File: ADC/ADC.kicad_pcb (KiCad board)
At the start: 2 copper layers, 57 x 82.4 mm, 78 parts, among them IC1 ADS7953SDBT, IC2 REF5025ID, IC3 ADS7953SDBT, IC4 REF5025ID, IC5 ADP3338AKCZ-5-REEL, J1 USB_C_Receptacle_USB2.0, J2 Conn_01x04_MountingPin, J3 Conn_02x11_Odd_Even, J4 Conn_02x08_Top_Bottom, J5 Conn_02x08_Top_Bottom, J6 Conn_01x04_MountingPin, J7 Conn_02x05_Odd_Even, U1 STM32F072CBT6, U2 OPA192ID, U3 PRTR5V0U2X, U4 XC6206PxxxMR-Regulator_Linear, U5 OPA192ID

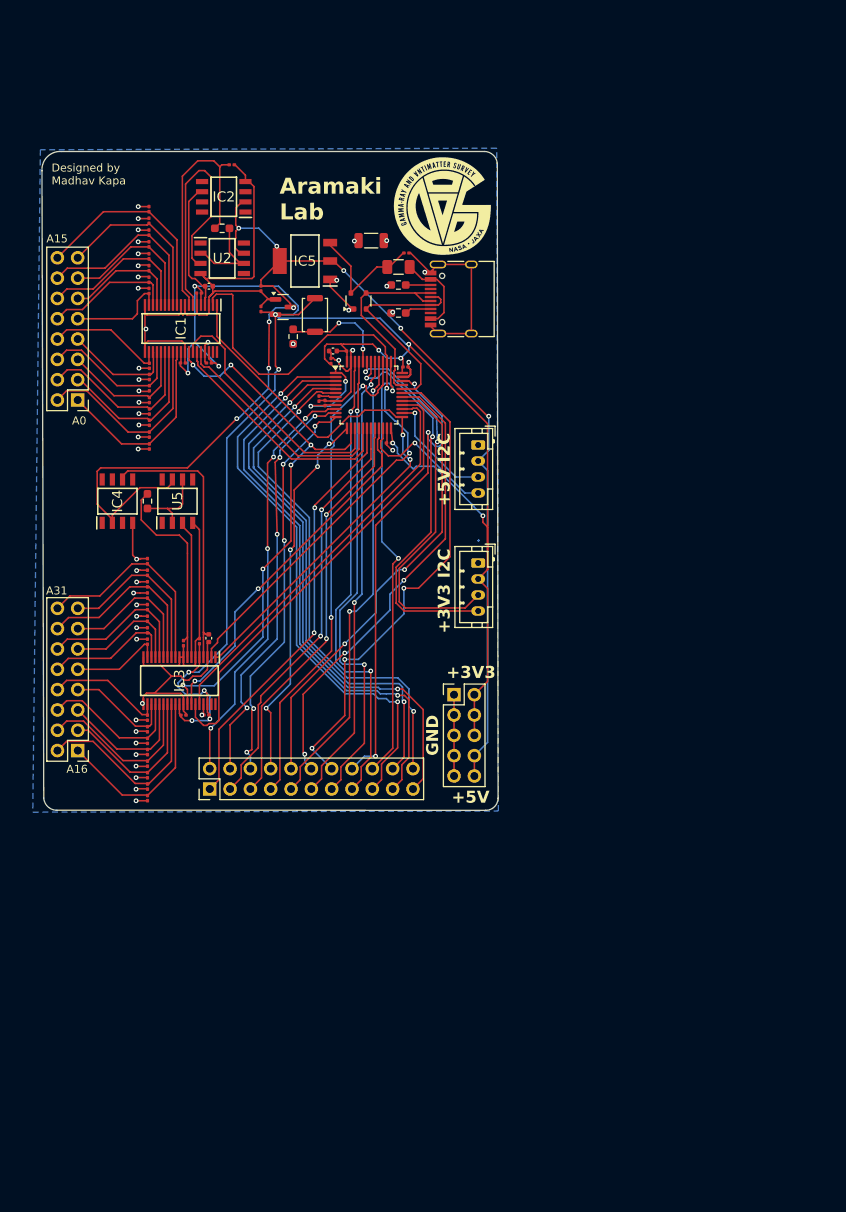
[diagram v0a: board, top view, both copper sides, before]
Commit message: updated schematic to match the eval kit
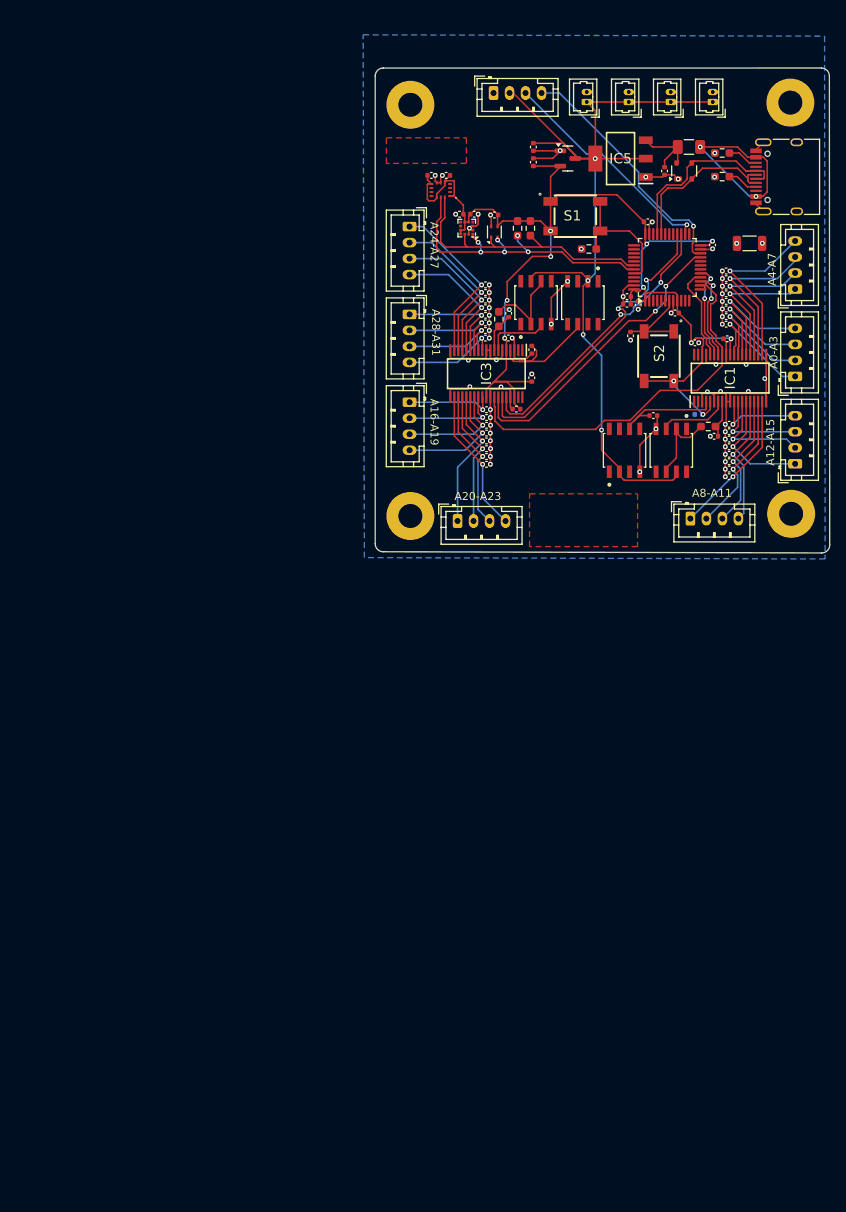
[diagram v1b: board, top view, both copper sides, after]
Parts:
- removed J3: Conn_02x11_Odd_Even, Connector_PinHeader_2.54mm:PinHeader_2x11_P2.54mm_Vertical
- removed J7: Conn_02x05_Odd_Even, Connector_PinHeader_2.54mm:PinHeader_2x05_P2.54mm_Vertical
- removed SW1: ~, Button_Switch_SMD:SW_Push_SPST_NO_Alps_SKRK
- added AC1: LSM6DSOTR, SamacSys_Parts:LGA-14_2.5X3X0.86_, F.Cu at (75.0, 34.2)
- added C53: 100nF, Capacitor_SMD:C_0402_1005Metric, F.Cu at (81.7, 37.4)
- added C54: 100nF, Capacitor_SMD:C_0402_1005Metric, F.Cu at (79.2, 37.2)
- added C56: 220nF, Capacitor_SMD:C_0402_1005Metric, F.Cu at (77.3, 37.2)
- added C57: 100nF, Capacitor_SMD:C_0402_1005Metric, F.Cu at (73.8, 32.4)
- added C58: 100nF, Capacitor_SMD:C_0402_1005Metric, F.Cu at (75.7, 32.4)
- added H1: MountingHole_Pad, MountingHole:MountingHole_3mm_Pad, F.Cu at (118.7, 23.3)
- added H2: MountingHole_Pad, MountingHole:MountingHole_3mm_Pad, F.Cu at (71.2, 75.0)
- added H3: MountingHole_Pad, MountingHole:MountingHole_3mm_Pad, F.Cu at (71.2, 23.6)
- added H4: MountingHole_Pad, MountingHole:MountingHole_3mm_Pad, F.Cu at (118.8, 74.7)
- added J10: Conn_01x04_MountingPin, Connector_JST:JST_PH_B4B-PH-K_1x04_P2.00mm_Vertical, F.Cu at (119.3, 68.5)
- added J11: Conn_01x04_MountingPin, Connector_JST:JST_PH_B4B-PH-K_1x04_P2.00mm_Vertical, F.Cu at (77.1, 75.6)
- added J12: Conn_01x04_MountingPin, Connector_JST:JST_PH_B4B-PH-K_1x04_P2.00mm_Vertical, F.Cu at (71.1, 60.8)
- added J13: Conn_01x04_MountingPin, Connector_JST:JST_PH_B4B-PH-K_1x04_P2.00mm_Vertical, F.Cu at (71.1, 38.8)
- added J14: Conn_01x04_MountingPin, Connector_JST:JST_PH_B4B-PH-K_1x04_P2.00mm_Vertical, F.Cu at (71.1, 49.8)
- added J15: Conn_01x02, Connector_Molex:Molex_PicoBlade_53047-0210_1x02_P1.25mm_Vertical, F.Cu at (103.8, 23.2)
- added J16: Conn_01x02, Connector_Molex:Molex_PicoBlade_53047-0210_1x02_P1.25mm_Vertical, F.Cu at (109.0, 23.2)
- added J8: Conn_01x04_MountingPin, Connector_JST:JST_PH_B4B-PH-K_1x04_P2.00mm_Vertical, F.Cu at (119.3, 46.6)
- added J9: Conn_01x04_MountingPin, Connector_JST:JST_PH_B4B-PH-K_1x04_P2.00mm_Vertical, F.Cu at (106.2, 75.3)
- added R6: 10k, Resistor_SMD:R_0603_1608Metric_Pad0.98x0.95mm_HandSolder, F.Cu at (86.2, 39.0)
- added R7: 10k, Resistor_SMD:R_0603_1608Metric_Pad0.98x0.95mm_HandSolder, F.Cu at (84.6, 39.0)
- added S1: SKQGABE010, SamacSys_Parts:SKQGAKE010, F.Cu at (91.8, 37.5)
- added S2: SKQGABE010, SamacSys_Parts:SKQGAKE010, F.Cu at (102.3, 55.0)
- added U6: SHT4x, Sensor_Humidity:Sensirion_DFN-4_1.5x1.5mm_P0.8mm_SHT4x_NoCentralPad, F.Cu at (81.7, 39.5)
- added U7: LIS3MDL, Package_LGA:LGA-12_2x2mm_P0.5mm, F.Cu at (78.2, 39.0)
- C1: footprint Capacitor_SMD:C_0201_0603Metric -> Capacitor_SMD:C_0402_1005Metric; moved to B.Cu
- C10, C11, C12, C13, C14, C15, C16, C17, C18, C19, C2, C20, C21, C22, C23, C24, C25, C26, C27, C28, C29, C3, C30, C31, C32, C33, C34, C35, C36, C37, C38, C39, C4, C40, C41, C42, C43, C44, C45, C46, C47, C48, C5, C50, C51, C6, C7, C8: footprint Capacitor_SMD:C_0201_0603Metric -> Capacitor_SMD:C_0402_1005Metric
- G***: moved to B.Cu
- J4, J5: value Conn_02x08_Top_Bottom -> Conn_01x02; footprint Connector_PinHeader_2.54mm:PinHeader_2x08_P2.54mm_Vertical -> Connector_Molex:Molex_PicoBlade_53047-0210_1x02_P1.25mm_Vertical
- moved J5 106.4 mm to (98.5, 23.2), turned to 90 degrees
- moved C14 77.3 mm to (111.0, 63.5), turned to 180 degrees
- moved C15 77.2 mm to (111.0, 64.4), turned to 180 degrees
- moved C16 77.0 mm to (111.0, 65.4), turned to 180 degrees
- moved C17 76.8 mm to (111.0, 66.3), turned to 180 degrees
- moved C18 76.6 mm to (111.0, 67.3), turned to 180 degrees
- moved C19 76.5 mm to (111.0, 68.2), turned to 180 degrees
- moved C20 76.3 mm to (111.0, 69.1), turned to 180 degrees
- moved C48 76.1 mm to (111.0, 70.1), turned to 180 degrees
- moved J4 73.7 mm to (93.2, 23.2), turned to 90 degrees
- moved C28 73.7 mm to (110.7, 51.0), turned to 180 degrees
- moved C27 73.6 mm to (110.7, 50.0), turned to 180 degrees
- moved C26 73.5 mm to (110.7, 49.1), turned to 180 degrees
- moved C25 73.4 mm to (110.7, 48.1), turned to 180 degrees
- moved C24 73.3 mm to (110.7, 47.2), turned to 180 degrees
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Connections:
- IC1 pad 1: RANGE_SEL -> unconnected-(IC1-GPIO2-Pad1)
- IC1 pad 2: POWER -> unconnected-(IC1-GPIO3-Pad2)
- IC3 pad 1: RANGE_SEL -> unconnected-(IC3-GPIO2-Pad1)
- IC3 pad 2: POWER -> unconnected-(IC3-GPIO3-Pad2)
- J2 pad 1: GND -> A0
- J2 pad 2: +3.3V -> A1
- J2 pad 3: SCL_I2C1 -> A2
- J2 pad 4: SDA_I2C1 -> A3
- J4 pad 1: A0 -> +5V
- J4 pad 2: A1 -> GND
- J5 pad 1: A16 -> +5V
- J5 pad 2: A17 -> GND
- U1 pad 25: RANGE_SEL -> /PB12
- U1 pad 38: POWER -> /PA15
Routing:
- net GND: track 239.6 -> 135.3 mm, vias 48 -> 71
- net +3.3V: track 256.4 -> 160.1 mm, vias 16 -> 11
- net POWER: track 84.0 -> 0.00 mm, vias 2 -> 0
- net RANGE_SEL: track 75.1 -> 0.00 mm, vias 2 -> 0
- net /PC13: track 72.2 -> 0.00 mm, vias 2 -> 0
- net /PC14: track 71.4 -> 0.00 mm, vias 2 -> 0
- net /PC15: track 70.7 -> 0.00 mm, vias 2 -> 0
- net /PF0: track 65.7 -> 0.00 mm, vias 2 -> 0
- net /PF1: track 64.3 -> 0.00 mm, vias 2 -> 0
- net /PB3: track 62.5 -> 0.00 mm, vias 2 -> 0
- net /PA10: track 61.0 -> 0.00 mm, vias 3 -> 0
- net /PA13: track 60.5 -> 0.00 mm, vias 3 -> 0
- net /PB9: track 59.1 -> 0.00 mm, vias 2 -> 0
- net /PB8: track 59.1 -> 0.00 mm, vias 2 -> 0
- net /PB4: track 58.4 -> 0.00 mm, vias 2 -> 0
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- added copper zone on F.Cu, net (none)
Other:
- board size 57 x 82.4 mm -> 56.8 x 60.6 mm
- board text added: "A0-A3"
- board text added: "A12-A15"
- board text added: "A16-A19"
- board text added: "A20-A23"
- board text added: "A24-A27"
- board text added: "A28-A31"
- board text added: "A4-A7"
- board text added: "A8-A11"
- board text removed: "+3V3"
- board text removed: "+3V3 I2C"
- board text removed: "+5V"
- board text removed: "+5V I2C"
- board text removed: "A0"
- board text removed: "A15"
- board text removed: "A16"
- board text removed: "A31"
- board text removed: "GND"

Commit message: finished V2
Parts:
- added C55: 100nF, Capacitor_SMD:C_0402_1005Metric, F.Cu at (70.7, 58.1)
- added C59: 1uF, Capacitor_SMD:C_0402_1005Metric, F.Cu at (73.6, 63.3)
- added C60: 1uF, Capacitor_SMD:C_0402_1005Metric, F.Cu at (34.9, 54.3)
- added C61: 100nF, Capacitor_SMD:C_0402_1005Metric, F.Cu at (57.4, 56.6)
- added C62: 100nF, Capacitor_SMD:C_0402_1005Metric, F.Cu at (49.1, 58.2)
- added C63: 10µF, Capacitor_SMD:C_0402_1005Metric, F.Cu at (37.6, 55.9)
- added R10: 33, Resistor_SMD:R_0402_1005Metric_Pad0.72x0.64mm_HandSolder, F.Cu at (66.4, 38.4)
- added R11: 33, Resistor_SMD:R_0402_1005Metric_Pad0.72x0.64mm_HandSolder, F.Cu at (66.4, 36.1)
- added R12: 33, Resistor_SMD:R_0402_1005Metric_Pad0.72x0.64mm_HandSolder, F.Cu at (59.7, 42.8)
- added R13: 33, Resistor_SMD:R_0402_1005Metric_Pad0.72x0.64mm_HandSolder, F.Cu at (59.7, 40.6)
- added R14: 33, Resistor_SMD:R_0402_1005Metric_Pad0.72x0.64mm_HandSolder, F.Cu at (59.7, 38.3)
- added R15: 33, Resistor_SMD:R_0402_1005Metric_Pad0.72x0.64mm_HandSolder, F.Cu at (59.7, 36.1)
- added R16: 33, Resistor_SMD:R_0402_1005Metric_Pad0.72x0.64mm_HandSolder, F.Cu at (73.3, 42.9)
- added R17: 33, Resistor_SMD:R_0402_1005Metric_Pad0.72x0.64mm_HandSolder, F.Cu at (73.3, 40.6)
- added R18: 33, Resistor_SMD:R_0402_1005Metric_Pad0.72x0.64mm_HandSolder, F.Cu at (73.3, 38.4)
- added R19: 33, Resistor_SMD:R_0402_1005Metric_Pad0.72x0.64mm_HandSolder, F.Cu at (73.3, 36.1)
- added R20: 33, Resistor_SMD:R_0402_1005Metric_Pad0.72x0.64mm_HandSolder, F.Cu at (80.5, 42.8)
- added R21: 33, Resistor_SMD:R_0402_1005Metric_Pad0.72x0.64mm_HandSolder, F.Cu at (80.5, 40.5)
- added R22: 33, Resistor_SMD:R_0402_1005Metric_Pad0.72x0.64mm_HandSolder, F.Cu at (80.5, 38.3)
- added R23: 33, Resistor_SMD:R_0402_1005Metric_Pad0.72x0.64mm_HandSolder, F.Cu at (80.5, 36.0)
- added R24: 33, Resistor_SMD:R_0402_1005Metric_Pad0.72x0.64mm_HandSolder, F.Cu at (52.2, 42.7)
- added R25: 33, Resistor_SMD:R_0402_1005Metric_Pad0.72x0.64mm_HandSolder, F.Cu at (52.2, 40.4)
- added R26: 33, Resistor_SMD:R_0402_1005Metric_Pad0.72x0.64mm_HandSolder, F.Cu at (52.2, 38.2)
- added R27: 33, Resistor_SMD:R_0402_1005Metric_Pad0.72x0.64mm_HandSolder, F.Cu at (52.2, 36.0)
- added R28: 33, Resistor_SMD:R_0402_1005Metric_Pad0.72x0.64mm_HandSolder, F.Cu at (45.3, 42.6)
- added R29: 33, Resistor_SMD:R_0402_1005Metric_Pad0.72x0.64mm_HandSolder, F.Cu at (45.3, 40.4)
- added R30: 33, Resistor_SMD:R_0402_1005Metric_Pad0.72x0.64mm_HandSolder, F.Cu at (45.3, 38.2)
- added R31: 33, Resistor_SMD:R_0402_1005Metric_Pad0.72x0.64mm_HandSolder, F.Cu at (45.3, 36.0)
- added R32: 33, Resistor_SMD:R_0402_1005Metric_Pad0.72x0.64mm_HandSolder, F.Cu at (38.4, 43.0)
- added R33: 33, Resistor_SMD:R_0402_1005Metric_Pad0.72x0.64mm_HandSolder, F.Cu at (38.4, 40.7)
- added R34: 33, Resistor_SMD:R_0402_1005Metric_Pad0.72x0.64mm_HandSolder, F.Cu at (38.4, 38.5)
- added R35: 33, Resistor_SMD:R_0402_1005Metric_Pad0.72x0.64mm_HandSolder, F.Cu at (38.4, 36.2)
- added R36: 33, Resistor_SMD:R_0402_1005Metric_Pad0.72x0.64mm_HandSolder, F.Cu at (31.4, 42.8)
- added R37: 33, Resistor_SMD:R_0402_1005Metric_Pad0.72x0.64mm_HandSolder, F.Cu at (31.4, 40.5)
- added R38: 33, Resistor_SMD:R_0402_1005Metric_Pad0.72x0.64mm_HandSolder, F.Cu at (31.4, 38.3)
- added R39: 33, Resistor_SMD:R_0402_1005Metric_Pad0.72x0.64mm_HandSolder, F.Cu at (31.4, 36.0)
- added R40: 33, Resistor_SMD:R_0402_1005Metric_Pad0.72x0.64mm_HandSolder, F.Cu at (57.2, 57.6)
- added R41: 33, Resistor_SMD:R_0402_1005Metric_Pad0.72x0.64mm_HandSolder, F.Cu at (48.1, 57.2)
- added R8: 33, Resistor_SMD:R_0402_1005Metric_Pad0.72x0.64mm_HandSolder, F.Cu at (66.4, 42.8)
- added R9: 33, Resistor_SMD:R_0402_1005Metric_Pad0.72x0.64mm_HandSolder, F.Cu at (66.4, 40.6)
- added SW1: SW_SPDT, Button_Switch_SMD:SW_SPDT_CK_JS102011SAQN, F.Cu at (29.0, 81.5)
- added TP10: TestPoint, TestPoint:TestPoint_Pad_D1.0mm, F.Cu at (52.3, 78.3)
- added TP11: TestPoint, TestPoint:TestPoint_Pad_D1.0mm, F.Cu at (36.0, 79.0)
- added TP12: TestPoint, TestPoint:TestPoint_Pad_D1.0mm, F.Cu at (36.0, 84.2)
- added TP4: TestPoint, TestPoint:TestPoint_Pad_D1.0mm, F.Cu at (62.8, 61.4)
- added TP9: TestPoint, TestPoint:TestPoint_Pad_D1.0mm, F.Cu at (52.0, 85.8)
- C1: value 1µF -> 100nF; moved to F.Cu
- C13, C14, C15, C16, C17, C18, C19, C20, C21, C22, C23, C24, C25, C26, C27, C28, C29, C30, C31, C32, C34, C35, C36, C37, C38, C39, C40, C41, C43, C44, C45, C46, C47, C48: value 150pF -> 270pF
- C2: value 1µF -> 100nF
- C50, C51: value 1µF -> 10uF
- C52: value 10µF -> 100nF
- G***: moved to F.Cu
- R1, R2, R3, R6, R7: footprint Resistor_SMD:R_0603_1608Metric_Pad0.98x0.95mm_HandSolder -> Resistor_SMD:R_0402_1005Metric_Pad0.72x0.64mm_HandSolder
- R4, R5: value 100 -> 33; footprint Resistor_SMD:R_0603_1608Metric_Pad0.98x0.95mm_HandSolder -> Resistor_SMD:R_0402_1005Metric_Pad0.72x0.64mm_HandSolder
- moved H1 113.7 mm to (27.0, 90.5)
- moved J1 100.0 mm to (26.1, 71.0), turned to -90 degrees
- moved R3 88.3 mm to (33.1, 72.8), turned to 180 degrees
- moved L1 87.3 mm to (29.4, 64.2), turned to 180 degrees
- moved R2 85.6 mm to (33.0, 69.7), turned to 180 degrees
- moved F1 85.3 mm to (41.1, 84.2), turned to 0 degrees
- moved C10 78.5 mm to (44.5, 84.2), turned to 0 degrees
- moved U3 77.6 mm to (39.7, 73.0), turned to 180 degrees
- moved IC5 69.9 mm to (46.8, 78.5), turned to 0 degrees
- moved J16 68.9 mm to (76.5, 84.0), turned to 0 degrees
- moved U4 68.4 mm to (48.8, 84.2), turned to 90 degrees
- moved C12 68.3 mm to (45.7, 85.5), turned to 0 degrees
- moved C11 67.7 mm to (45.8, 83.0), turned to 0 degrees
- moved J8 63.6 mm to (55.9, 42.3)
- moved H2 62.7 mm to (27.0, 30.5)
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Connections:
- F1 pad 1: VBUS -> VBUS_IN
- H4 pad 1: (no net) -> GND
- IC1 pad 34: MISO_SPI1 -> Net-(IC1-SDO)
- IC3 pad 34: MISO_SPI2 -> Net-(IC3-SDO)
- J10 pad 1: A12 -> Net-(J10-Pin_1)
- J10 pad 2: A13 -> Net-(J10-Pin_2)
- J10 pad 3: A14 -> Net-(J10-Pin_3)
- J10 pad 4: A15 -> Net-(J10-Pin_4)
- J11 pad 1: A20 -> Net-(J11-Pin_1)
- J11 pad 2: A21 -> Net-(J11-Pin_2)
- J11 pad 3: A22 -> Net-(J11-Pin_3)
- J11 pad 4: A23 -> Net-(J11-Pin_4)
- J12 pad 1: A16 -> Net-(J12-Pin_1)
- J12 pad 2: A17 -> Net-(J12-Pin_2)
- J12 pad 3: A18 -> Net-(J12-Pin_3)
- J12 pad 4: A19 -> Net-(J12-Pin_4)
- J13 pad 1: A24 -> Net-(J13-Pin_1)
- J13 pad 2: A25 -> Net-(J13-Pin_2)
- J13 pad 3: A26 -> Net-(J13-Pin_3)
- J13 pad 4: A27 -> Net-(J13-Pin_4)
- J14 pad 1: A28 -> Net-(J14-Pin_1)
- J14 pad 2: A29 -> Net-(J14-Pin_2)
- J14 pad 3: A30 -> Net-(J14-Pin_3)
- J14 pad 4: A31 -> Net-(J14-Pin_4)
- J15 pad 1: +5V -> GND
- J15 pad 2: GND -> +5V
- J16 pad 1: +5V -> GND
- J16 pad 2: GND -> +5V
- J2 pad 1: A0 -> Net-(J2-Pin_1)
- J2 pad 2: A1 -> Net-(J2-Pin_2)
- J2 pad 3: A2 -> Net-(J2-Pin_3)
- J2 pad 4: A3 -> Net-(J2-Pin_4)
- J4 pad 1: +5V -> GND
- J4 pad 2: GND -> +5V
- J5 pad 1: +5V -> GND
- J5 pad 2: GND -> +5V
- J8 pad 1: A4 -> Net-(J8-Pin_1)
- J8 pad 2: A5 -> Net-(J8-Pin_2)
- J8 pad 3: A6 -> Net-(J8-Pin_3)
- J8 pad 4: A7 -> Net-(J8-Pin_4)
- J9 pad 1: A8 -> Net-(J9-Pin_1)
- J9 pad 2: A9 -> Net-(J9-Pin_2)
- J9 pad 3: A10 -> Net-(J9-Pin_3)
- J9 pad 4: A11 -> Net-(J9-Pin_4)
- U1 pad 10: /PA0 -> unconnected-(U1-PA0-Pad10)
- U1 pad 11: /PA1 -> unconnected-(U1-PA1-Pad11)
- U1 pad 12: /PA2 -> unconnected-(U1-PA2-Pad12)
- U1 pad 13: /PA3 -> unconnected-(U1-PA3-Pad13)
- U1 pad 18: /PB0 -> unconnected-(U1-PB0-Pad18)
- U1 pad 19: /PB1 -> unconnected-(U1-PB1-Pad19)
- U1 pad 2: /PC13 -> unconnected-(U1-PC13-Pad2)
- U1 pad 20: /PB2 -> unconnected-(U1-PB2-Pad20)
- U1 pad 25: /PB12 -> unconnected-(U1-PB12-Pad25)
- U1 pad 29: /PA8 -> unconnected-(U1-PA8-Pad29)
- U1 pad 3: /PC14 -> unconnected-(U1-PC14-Pad3)
- U1 pad 30: /PA9 -> unconnected-(U1-PA9-Pad30)
- U1 pad 31: /PA10 -> unconnected-(U1-PA10-Pad31)
- U1 pad 34: /PA13 -> unconnected-(U1-PA13-Pad34)
- U1 pad 37: /PA14 -> unconnected-(U1-PA14-Pad37)
- U1 pad 38: /PA15 -> unconnected-(U1-PA15-Pad38)
- U1 pad 39: /PB3 -> unconnected-(U1-PB3-Pad39)
- U1 pad 4: /PC15 -> unconnected-(U1-PC15-Pad4)
- U1 pad 40: /PB4 -> unconnected-(U1-PB4-Pad40)
- U1 pad 41: /PB5 -> unconnected-(U1-PB5-Pad41)
- U1 pad 45: /PB8 -> unconnected-(U1-PB8-Pad45)
- U1 pad 46: /PB9 -> unconnected-(U1-PB9-Pad46)
- U1 pad 5: /PF0 -> unconnected-(U1-PF0-Pad5)
- U1 pad 6: /PF1 -> unconnected-(U1-PF1-Pad6)
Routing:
- net GND: track 135.3 -> 97.6 mm, vias 71 -> 259
- net +5V: track 111.6 -> 135.5 mm, vias 4 -> 10
- net A27: track 16.8 -> 39.7 mm, vias 1 -> 2
- net A31: track 11.8 -> 34.2 mm, vias 1 -> 2
- net SCL_I2C1: track 39.9 -> 17.6 mm, vias 6 -> 0
- net A30: track 12.6 -> 32.3 mm, vias 1 -> 2
- net MOSI_SPI2: track 38.4 -> 20.4 mm, vias 2 -> 0
- net A29: track 13.5 -> 30.7 mm, vias 1 -> 2
- net A19: track 15.1 -> 31.3 mm, vias 1 -> 2
- net A26: track 18.5 -> 34.5 mm, vias 1 -> 2
- net A28: track 14.0 -> 29.8 mm, vias 1 -> 2
- net SCK_SPI2: track 37.5 -> 22.0 mm, vias 2 -> 0
- net A15: track 11.1 -> 26.2 mm, vias 1 -> 2
- net A23: track 18.1 -> 33.0 mm, vias 1 -> 2
- net A22: track 17.6 -> 32.3 mm, vias 1 -> 2
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- added copper zone on F.Cu, net GND
- removed copper zone on F.Cu, net (none)
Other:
- board size 56.8 x 60.6 mm -> 60.4 x 70.3 mm
- board text removed: "A0-A3"
- board text removed: "A12-A15"
- board text removed: "A16-A19"
- board text removed: "A20-A23"
- board text removed: "A24-A27"
- board text removed: "A28-A31"
- board text removed: "A4-A7"
- board text removed: "A8-A11"

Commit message: updated v2
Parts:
- removed TP4: TestPoint, TestPoint:TestPoint_Pad_D1.0mm
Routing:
- net GND: vias 259 -> 258
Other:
- board text added: "A0-3"
- board text added: "A12-15"
- board text added: "A16-19"
- board text added: "A20-23"
- board text added: "A24-27"
- board text added: "A28-31"
- board text added: "A4-7"
- board text added: "A8-11"
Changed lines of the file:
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@@
 		)
 	)
-	(footprint "TestPoint:TestPoint_Pad_D1.0mm"
-		(layer "F.Cu")
-		(at 62.83 61.41)
-		(descr "SMD pad as test Point, diameter 1.0mm")
-		(tags "test point SMD pad")
-		(property "Reference" "TP4"
-			(at 0 -1.448 0)
-			(layer "F.SilkS")
-			(hide yes)
-			(effects
-				(font
-					(size 1 1)
-					(thickness 0.15)
-				)
-			)
-		)
-		(property "Value" "TestPoint"
-			(at 0 1.55 0)
-			(layer "F.Fab")
-			(hide yes)
-			(effects
-				(font
-					(size 1 1)
-					(thickness 0.15)
-				)
-			)
-		)
-		(property "Footprint" "TestPoint:TestPoint_Pad_D1.0mm"
-			(at 0 0 0)
-			(unlocked yes)
-			(layer "F.Fab")
-			(hide yes)
-			(effects
-				(font
-					(size 1.27 1.27)
-					(thickness 0.15)
-				)
-			)
-		)
-		(property "Datasheet" ""
-			(at 0 0 0)
-			(unlocked yes)
-			(layer "F.Fab")
-			(hide yes)
-			(effects
-				(font
-					(size 1.27 1.27)
-					(thickness 0.15)
-				)
-			)
-		)
-		(property "Description" "test point"
-			(at 0 0 0)
-			(unlocked yes)
-			(layer "F.Fab")
-			(hide yes)
-			(effects
-				(font
-					(size 1.27 1.27)
-					(thickness 0.15)
-				)
-			)
-		)
-		(property ki_fp_filters "Pin* Test*")
-		(sheetname "Root")
-		(sheetfile "ADC.kicad_sch")
-		(attr exclude_from_pos_files)
-		(fp_circle
-			(center 0 0)
-			(end 0 0.7)
-			(stroke
-				(width 0.12)
-				(type solid)
-			)
-			(fill none)
-			(layer "F.SilkS")
-		)
-		(fp_circle
-			(center 0 0)
-			(end 1 0)
-			(stroke
-				(width 0.05)
-				(type solid)
-			)
-			(fill none)
-			(layer "F.CrtYd")
-		)
-		(pad "1" smd circle
-			(at 0 0)
-			(size 1 1)
-			(layers "F.Cu" "F.Mask")
-			(net 52 "CS_SPI")
-			(pinfunction "1")
-			(pintype "passive")
-		)
-	)
 	(footprint "Connector_JST:JST_PH_B4B-PH-K_1x04_P2.00mm_Vertical"
 		(layer "F.Cu")
@@
 		(layer "Edge.Cuts")
 	)
+	(gr_text "A12-15"
+		(at 74.25 46.2 0)
+		(layer "F.SilkS")
+		(effects
+			(font
+				(size 1 1)
+				(thickness 0.25)
+				(bold yes)
+			)
+			(justify left bottom)
+		)
+	)
+	(gr_text "A4-7"
+		(at 54.15 46.2 0)
+		(layer "F.SilkS")
+		(effects
+			(font
+				(size 1 1)
+				(thickness 0.25)
+				(bold yes)
+			)
+			(justify left bottom)
+		)
+	)
+	(gr_text "A24-27"
+		(at 32 46.25 0)
+		(layer "F.SilkS")
+		(effects
+			(font
+				(size 1 1)
+				(thickness 0.25)
+				(bold yes)
+			)
+			(justify left bottom)
+		)
+	)
+	(gr_text "A20-23"
+		(at 38.9 46.3 0)
+		(layer "F.SilkS")
+		(effects
+			(font
+				(size 1 1)
+				(thickness 0.25)
+				(bold yes)
+			)
+			(justify left bottom)
+		)
+	)
+	(gr_text "A8-11"
+		(at 67.55 46.15 0)
+		(layer "F.SilkS")
+		(effects
+			(font
+				(size 1 1)
+				(thickness 0.25)
+				(bold yes)
+			)
+			(justify left bottom)
+		)
+	)
+	(gr_text "A0-3"
+		(at 61.05 46.2 0)
+		(layer "F.SilkS")
+		(effects
+			(font
+				(size 1 1)
+				(thickness 0.25)
+				(bold yes)
+			)
+			(justify left bottom)
+		)
+	)
+	(gr_text "A28-31"
+		(at 25.05 46.35 0)
+		(layer "F.SilkS")
+		(effects
+			(font
+				(size 1 1)
+				(thickness 0.25)
+				(bold yes)
+			)
+			(justify left bottom)
+		)
+	)
+	(gr_text "A16-19"
+		(at 45.9 46.25 0)
+		(layer "F.SilkS")
+		(effects
+			(font
+				(size 1 1)
+				(thickness 0.25)
+				(bold yes)
+			)
+			(justify left bottom)
+		)
+	)
 	(gr_text "Designed by\nMadhav Kapa"
 		(at 57.99 92.28 0)
@@
 	)
 	(via
-		(at 54.662 50.09)
-		(size 0.6)
-		(drill 0.3)
-		(layers "F.Cu" "B.Cu")
-		(net 1)
-	)
-	(via
 		(at 24.444514 58.264991)
 		(size 0.6)
@@
 	(segment
 		(start 61.973061 61.622815)
-		(end 62.452185 61.622815)
+		(end 62.327185 61.622815)
 		(width 0.2)
 		(layer "F.Cu")
@@
 	)
 	(segment
-		(start 62.452185 61.622815)
-		(end 63.005 61.07)
+		(start 59.95 64.3875)
+		(end 59.95 63.645876)
 		(width 0.2)
 		(layer "F.Cu")
@@
 	)
 	(segment
-		(start 63.005 61.07)
+		(start 63.005 60.945)
 		(end 63.005 57.33)
 		(width 0.2)
@@
 	)
 	(segment
+		(start 62.327185 61.622815)
+		(end 63.005 60.945)
+		(width 0.2)
+		(layer "F.Cu")
+		(net 52)
+	)
+	(segment
 		(start 44.578944 58.971056)
 		(end 44.17 59.38)
@@
 	)
 	(segment
-		(start 59.95 63.645876)
-		(end 61.973061 61.622815)
-		(width 0.2)
-		(layer "F.Cu")
-		(net 52)
-	)
-	(segment
 		(start 44.578944 58.944882)
 		(end 44.578944 58.971056)
@@
 	)
 	(segment
-		(start 59.95 64.3875)
-		(end 59.95 63.645876)
+		(start 59.95 63.645876)
+		(end 61.973061 61.622815)
 		(width 0.2)
 		(layer "F.Cu")
@@
 	)
 	(segment
-		(start 62.625 60.470874)
-		(end 62.625 57.5)
+		(start 59.45 63.425)
+		(end 61.632185 61.242815)
 		(width 0.2)
 		(layer "F.Cu")
@@
 	)
 	(segment
-		(start 62.625 57.5)
-		(end 61.825 56.7)
+		(start 61.853059 61.242815)
+		(end 62.625 60.470874)
 		(width 0.2)
 		(layer "F.Cu")
@@
 	)
 	(segment
-		(start 61.632185 61.242815)
-		(end 61.853059 61.242815)
+		(start 59.45 64.3875)
+		(end 59.45 63.425)
 		(width 0.2)
 		(layer "F.Cu")
@@
 	)
 	(segment
-		(start 59.45 64.3875)
-		(end 59.45 63.425)
+		(start 62.625 57.5)
+		(end 61.825 56.7)
 		(width 0.2)
 		(layer "F.Cu")
@@
 	)
 	(segment
-		(start 59.45 63.425)
-		(end 61.632185 61.242815)
+		(start 62.625 60.470874)
+		(end 62.625 57.5)
 		(width 0.2)
 		(layer "F.Cu")
@@
 	)
 	(segment
-		(start 61.853059 61.242815)
-		(end 62.625 60.470874)
+		(start 61.632185 61.242815)
+		(end 61.853059 61.242815)
 		(width 0.2)
 		(layer "F.Cu")

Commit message: pcb update
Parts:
- removed S1, S2: SKQGABE010, SamacSys_Parts:SKQGAKE010
- added SW2: SW_Push, Button_Switch_SMD:SW_Push_SPST_NO_Alps_SKRK, F.Cu at (69.8, 69.9)
- added SW3: SW_Push, Button_Switch_SMD:SW_Push_SPST_NO_Alps_SKRK, F.Cu at (62.0, 77.3)
- C11, C12, C33, C42: value 1µF -> 1uF
- C49, C63, C9: value 10µF -> 10uF
- U4: value XC6206PxxxMR-Regulator_Linear -> XC6206P332PR-G
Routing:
- net +3.3V: track 162.9 -> 159.9 mm
- net NRST: track 11.1 -> 9.65 mm
- net BOOT0: track 8.50 -> 9.08 mm
